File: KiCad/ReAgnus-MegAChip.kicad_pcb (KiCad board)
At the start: 4 copper layers, 78 x 49 mm, 55 parts, among them J1 Conn_02x05_Odd_Even, J2 Conn_02x02_Odd_Even, J3 Conn_01x03, J4 Conn_01x01, U1 PLCC-84-Plug, U11 74LVC245A, U12 74LVC1GX04, U13 TPS73643DBV, U2 LM1117-3.3, U3 SN74CBT16210, U4 SN74CBT16210, U5 SN74CBT16210, U6 SN74CBT16210, U7 GW1N-UV9LQ144, U8 74LVC1G07, U9 Agnus_TH_plug_pins, Y1 CL=16pF

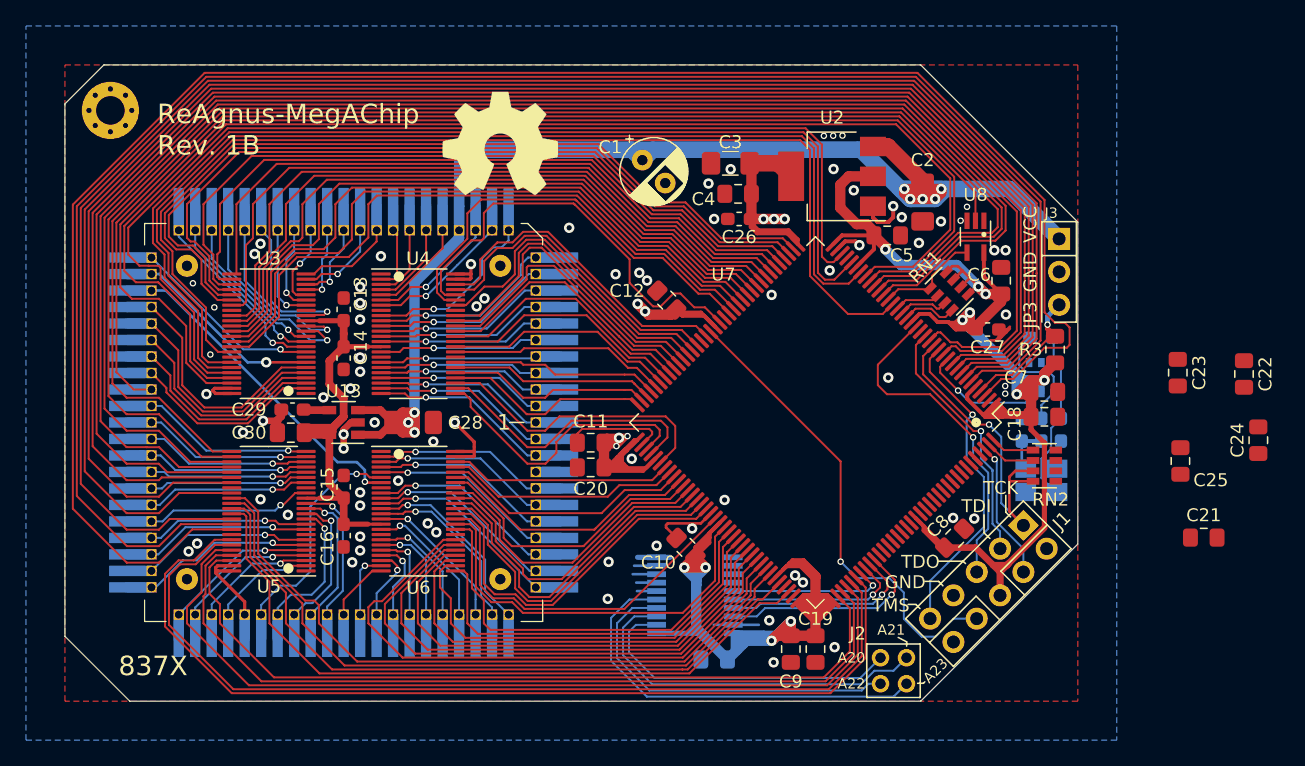
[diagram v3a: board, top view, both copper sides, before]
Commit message: Went to a 4-layer PCB and changed FPGA to GW1NR-UV9LQ144P with embedded PSRAM, changed FET-bus-switches to SN74CBT16210CDGVR (TVSOP-48) and added 4.3V LDO regulator TPS73643DBV and re-routed.
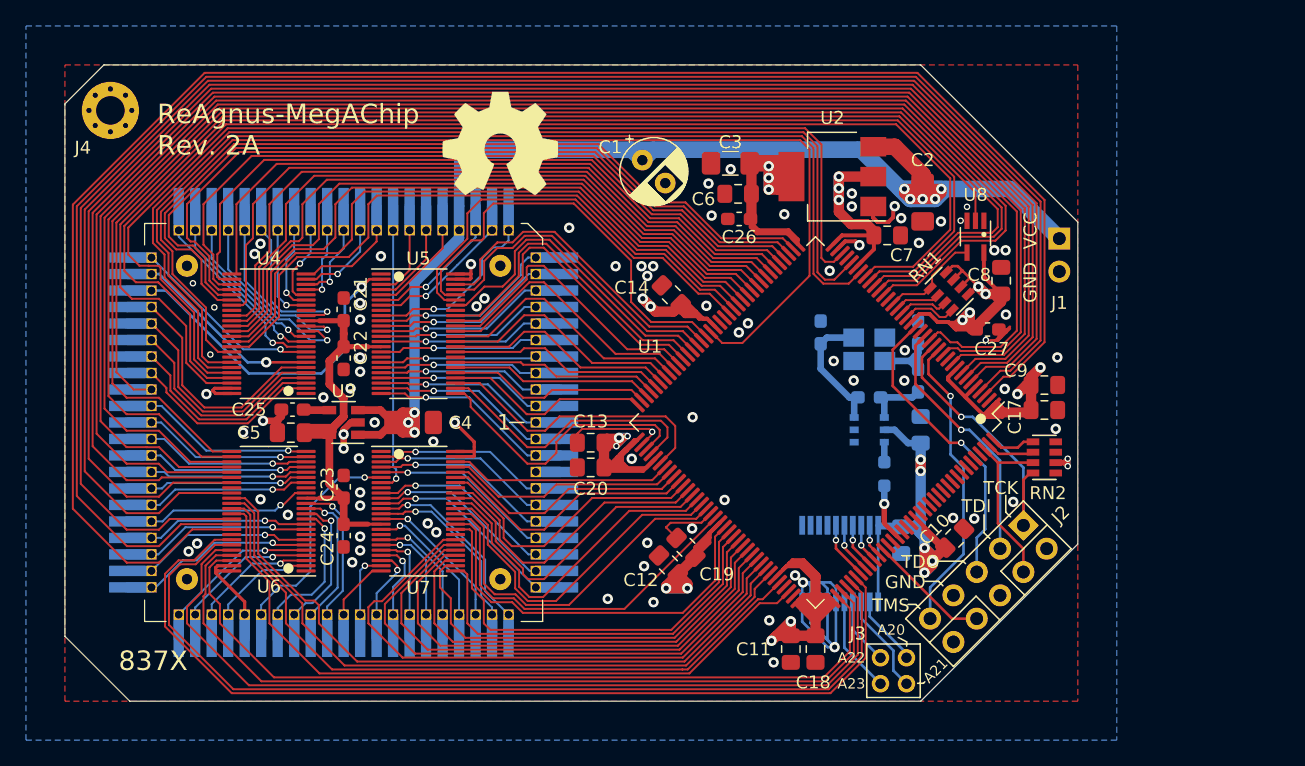
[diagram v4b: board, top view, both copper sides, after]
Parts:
- removed the C10 at (165.1, 124.5)
- removed the C11 at (157.8, 116.4)
- removed the C18 at (192.7, 114.4)
- removed the C23 at (203.0, 111.0)
- removed the C24 at (209.2, 116.2)
- removed the C25 at (203.2, 117.8)
- removed the C7 at (192.7, 112.5)
- removed the J3 at (193.9, 100.7)
- removed the U11 at (165.8, 128.1)
- removed the U12 at (192.5, 111.4)
- removed the U7 at (175.1, 114.8)
- added C13: 0.1uF, Capacitor_SMD:C_0805_2012Metric_Pad1.15x1.40mm_HandSolder, F.Cu at (157.8, 116.4)
- added C14: 0.1uF, Capacitor_SMD:C_0805_2012Metric_Pad1.15x1.40mm_HandSolder, F.Cu at (164.0, 105.0)
- added C15: 0.1uF, Capacitor_SMD:C_0805_2012Metric_Pad1.15x1.40mm_HandSolder, B.Cu at (181.7, 123.9)
- added C9: 0.1uF, Capacitor_SMD:C_0805_2012Metric_Pad1.15x1.40mm_HandSolder, F.Cu at (192.7, 112.0)
- added J1: Conn_01x02, Connector_PinHeader_2.54mm:PinHeader_1x02_P2.54mm_Vertical, F.Cu at (193.9, 100.7)
- added U1: GW1NR-UV9LQ144P, Package_QFP:LQFP-144_20x20mm_P0.5mm, F.Cu at (175.1, 114.8)
- added U10: 74LVC245A, Package_SO:TSSOP-20_4.4x6.5mm_P0.65mm, B.Cu at (177.0, 125.7)
- added U9: 74LVC1GX04, Package_SO:TSOP-6_1.65x3.05mm_P0.95mm, B.Cu at (179.2, 115.4)
- C16: renamed from C21; value 0.01uF -> 0.1uF; moved to B.Cu
- C17: value 0.1uF -> 0.01uF; moved to F.Cu
- C21: renamed from C13; value 0.1uF -> 0.1uF (0603)
- C22: renamed from C14; value 0.1uF -> 0.1uF (0603)
- C23: renamed from C15; value 0.1uF -> 0.1uF (0603)
- C24: renamed from C16; value 0.1uF -> 0.1uF (0603)
- C5: renamed from C30; value 10uF -> 1uF
- R3: value R_Small -> 33Ω; footprint Resistor_SMD:R_0805_2012Metric_Pad1.15x1.40mm_HandSolder -> Resistor_SMD:R_0603_1608Metric_Pad0.98x0.95mm_HandSolder; moved to B.Cu
- RN1, RN2: value R_Pack04 -> 4.7k
- moved C19 45.0 mm to (165.1, 124.5), turned to 135 degrees
- moved C17 31.9 mm to (192.7, 113.9), turned to 0 degrees
- moved C16 23.3 mm to (183.2, 115.4), turned to 90 degrees
- moved C12 20.4 mm to (163.8, 125.8)
- moved C29 20.0 mm to (175.5, 107.9), turned to 90 degrees
- moved Y1 16.7 mm to (179.2, 109.2), turned to 180 degrees
- moved R3 16.3 mm to (180.4, 118.8), turned to 270 degrees
- moved R2 14.0 mm to (179.2, 112.9), turned to 180 degrees
- moved C28 11.0 mm to (183.0, 107.9)
- moved R1 10.2 mm to (183.0, 111.6), turned to 90 degrees
- moved RN2 0.64 mm to (192.7, 117.5)
- renumbered C8 to C10, C9 to C11, C19 to C18, C22 to C19, C29 to C25, C41 to C28, C40 to C29, C28 to C4, C4 to C6, C5 to C7, C6 to C8, J1 to J2, J2 to J3, U1 to U11, U9 to U12, U13 to U3, U3 to U4, U4 to U5, U5 to U6, U6 to U7
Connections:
- J2 pad 4: JP1 -> nNTSC
- J2 pad 8: JP2 -> JP1
- J3 pad 1: A20 -> A22
- J3 pad 2: A21 -> A20
- J3 pad 3: A22 -> A23
- J3 pad 4: A23 -> A21
- R3 pad 1: 3V3 -> Net-(R3-Pad1)
- R3 pad 2: JP3 -> GCLKT_1
- RN2 pad 3: TCK -> nNTSC
- RN2 pad 6: GND -> 3V3
- U5 pad 2: BLISS -> XCLK|A20
- U5 pad 46: BLISS_3V3 -> XCLK|A20_3V3
- U7 pad 40: XCLK|A20_3V3 -> BLISS_3V3
- U7 pad 7: XCLK|A20 -> BLISS
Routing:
- net JP2: track 36.5 -> 0.00 mm, vias 1 -> 0
- net 3V3: track 288.6 -> 262.3 mm, vias 19 -> 28
- net A23: track 31.7 -> 7.46 mm
- net A22: track 27.8 -> 5.19 mm
- net A21: track 28.7 -> 7.75 mm
- net GND: track 65.7 -> 86.3 mm, vias 76 -> 85
- net A20: track 24.8 -> 5.48 mm
- net BLISS: track 6.88 -> 22.8 mm, vias 0 -> 1
- net nNTSC: track 0.00 -> 13.4 mm
- net A20_3V3: track 16.4 -> 3.08 mm
- net A21_3V3: track 15.0 -> 3.52 mm
- net JP3: track 10.6 -> 0.00 mm, vias 1 -> 0
- net GCLKT_7: track 9.71 -> 0.00 mm, vias 1 -> 0
- net A22_3V3: track 13.6 -> 4.00 mm
- net GCLKT_1: track 0.00 -> 8.58 mm, vias 0 -> 1
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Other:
- board text added: "(C) 2022, 2024 Design by J.Bilander"
- board text added: "33Ω"
- board text added: "ReAgnus-MegAChip Rev. 2A"
- board text removed: "(C) 2022 Design by J.Bilander"
- board text removed: "JP3"
- board text removed: "ReAgnus-MegAChip Rev. 1B"

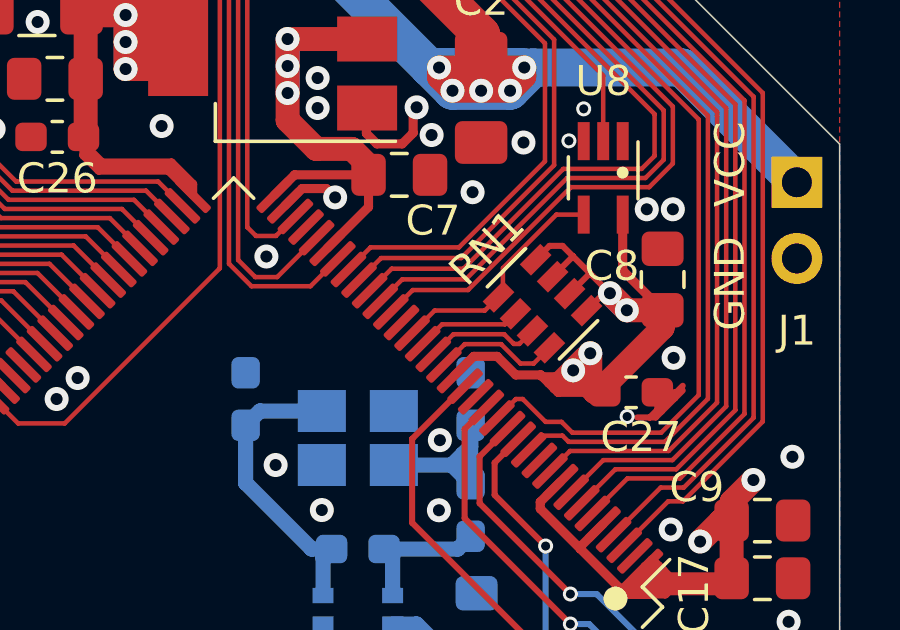
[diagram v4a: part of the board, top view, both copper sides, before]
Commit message: Moved signal nNTSC_8372_3V3 to pin FPGA pin 24
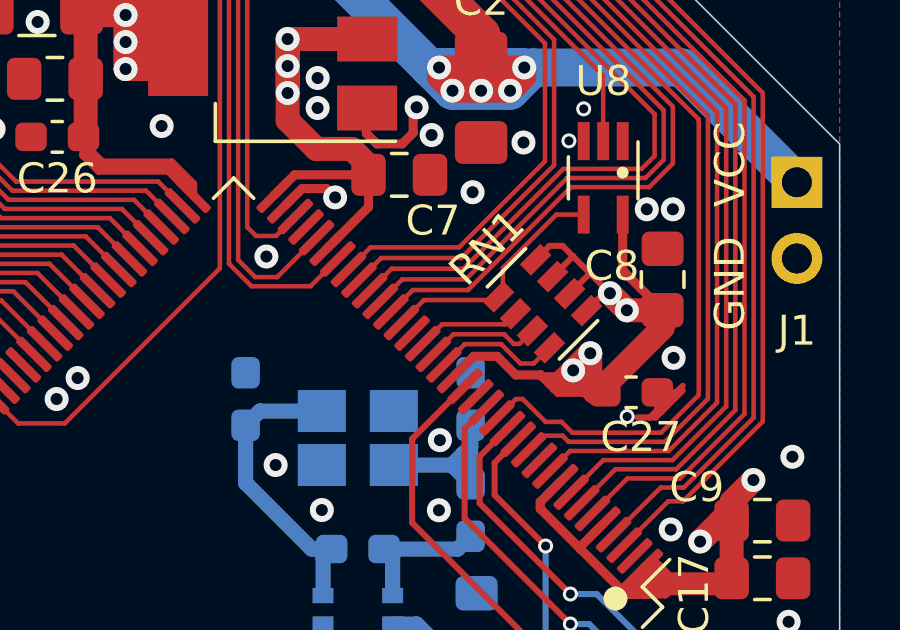
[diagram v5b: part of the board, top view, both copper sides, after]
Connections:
- U1 pad 23: nNTSC_8372_3V3 -> Net-(U1-Pad23)
- U1 pad 24: Net-(U1-Pad24) -> nNTSC_8372_3V3

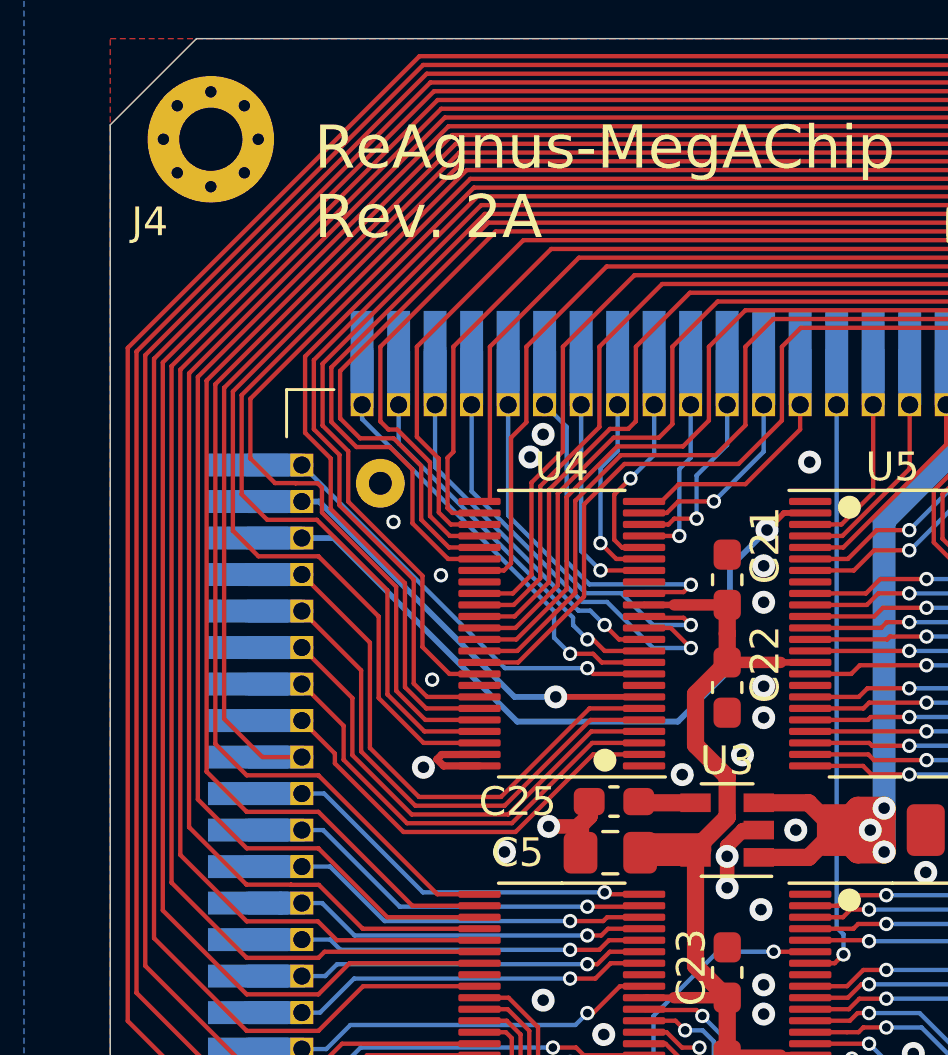
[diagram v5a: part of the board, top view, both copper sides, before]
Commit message: Added a pull-up resistor R4 for pin 41 (PAL/NTSC-selector) because A500 Rev.6A doesn't have pull-up on motherboard, and bumped to Rev. 2B
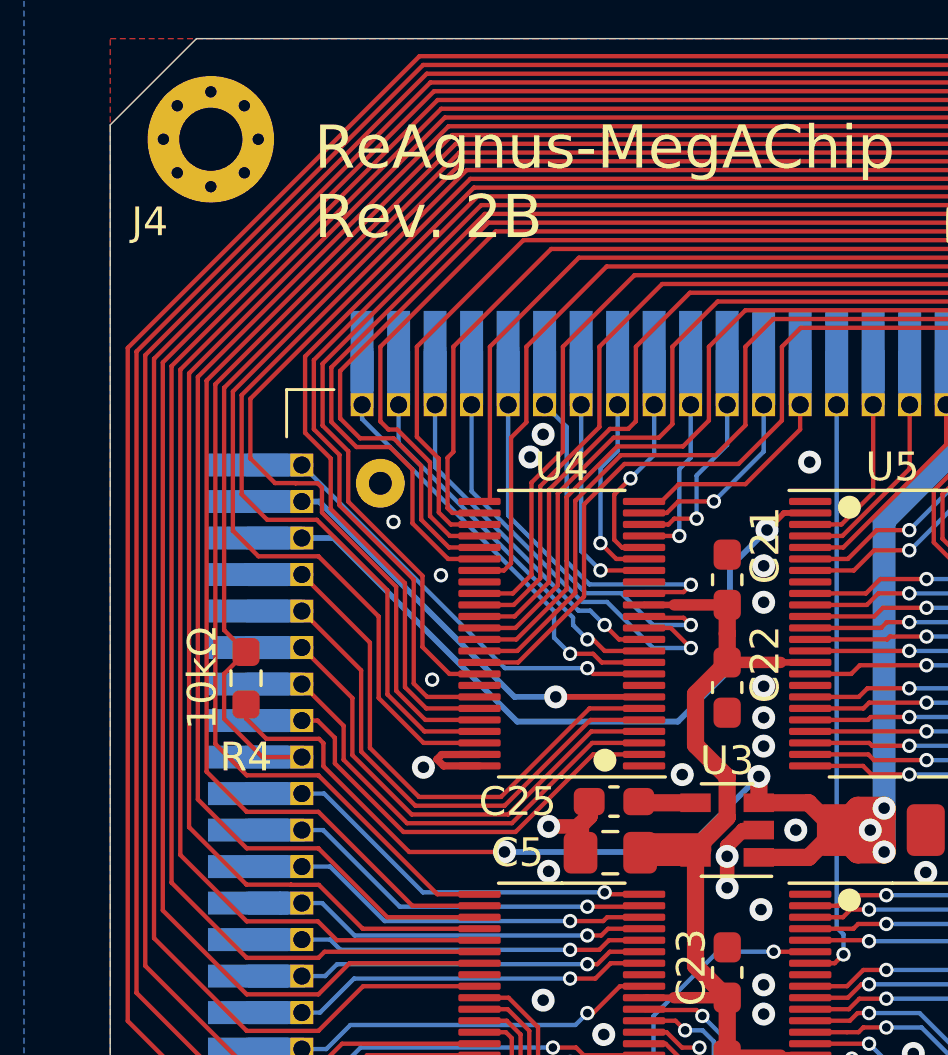
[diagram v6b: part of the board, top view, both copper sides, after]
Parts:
- added R4: 10kΩ, Resistor_SMD:R_0603_1608Metric_Pad0.98x0.95mm_HandSolder, F.Cu at (122.0, 109.6)
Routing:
- net VCC: track 146.4 -> 169.1 mm, vias 8 -> 10
- net GND|nNTSC_8372: track 90.8 -> 91.4 mm
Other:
- board text added: "10kΩ"
- board text added: "ReAgnus-MegAChip Rev. 2B"
- board text removed: "ReAgnus-MegAChip Rev. 2A"

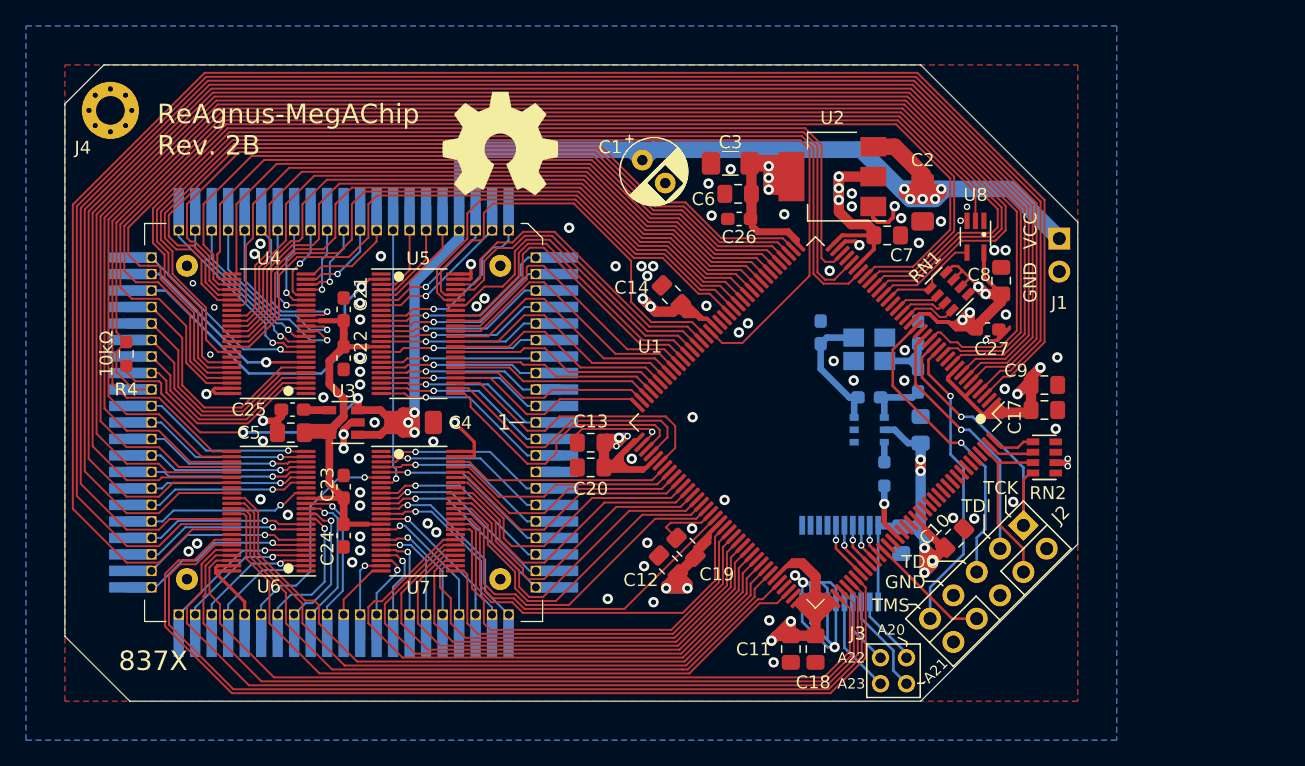
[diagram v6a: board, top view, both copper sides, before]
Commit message: Moved signals from bank 3 to bank 0
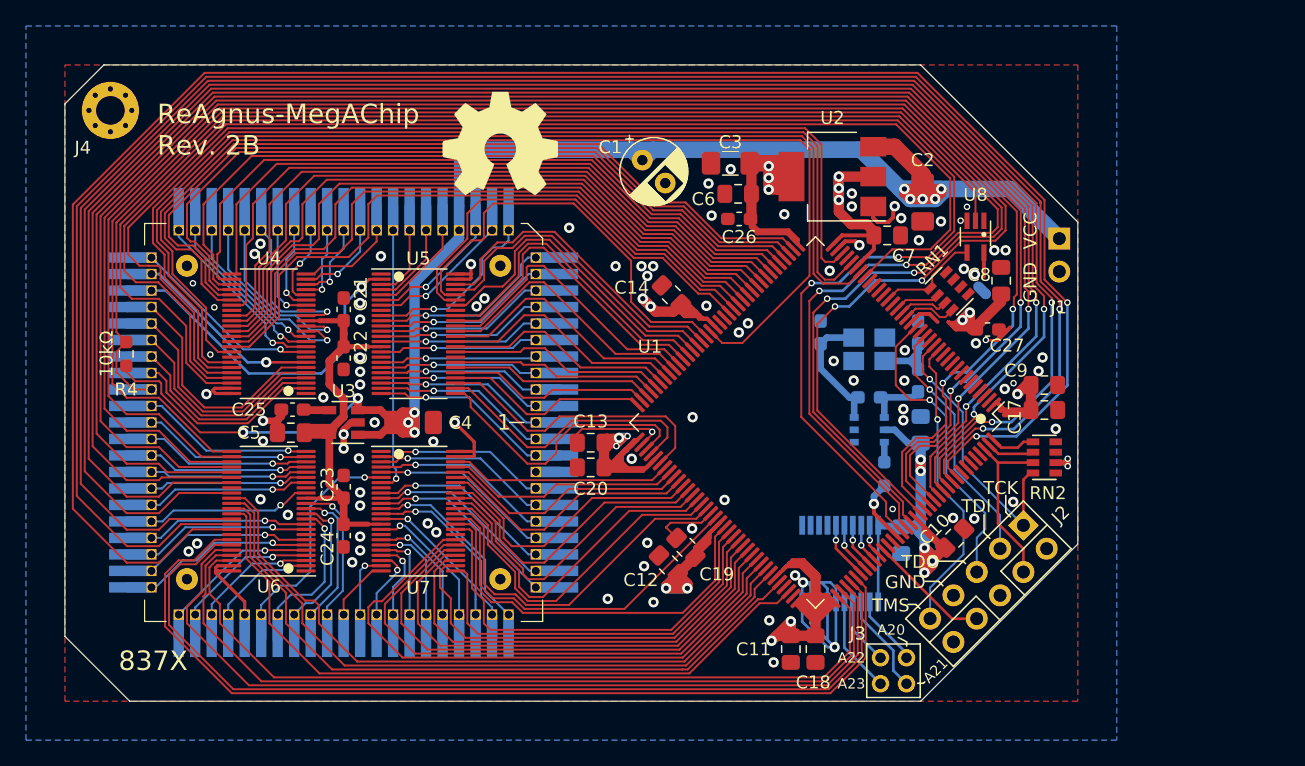
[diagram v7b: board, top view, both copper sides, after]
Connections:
- U1 pad 10: DRA5|DRA4_3V3 -> Net-(U1-Pad10)
- U1 pad 12: DRA4|DRA3_3V3 -> Net-(U1-Pad12)
- U1 pad 124: Net-(U1-Pad124) -> 14M|CCK_3V3
- U1 pad 125: Net-(U1-Pad125) -> DRA0_3V3|GND
- U1 pad 126: Net-(U1-Pad126) -> DRA1|DRA0_3V3
- U1 pad 128: Net-(U1-Pad128) -> DRA2|DRA1_3V3
- U1 pad 129: Net-(U1-Pad129) -> DRA3|DRA2_3V3
- U1 pad 130: Net-(U1-Pad130) -> DRA4|DRA3_3V3
- U1 pad 131: Net-(U1-Pad131) -> DRA5|DRA4_3V3
- U1 pad 132: Net-(U1-Pad132) -> DRA6|DRA5_3V3
- U1 pad 133: Net-(U1-Pad133) -> DRA7|DRA6_3V3
- U1 pad 134: Net-(U1-Pad134) -> DRA8|DRA7_3V3
- U1 pad 135: Net-(U1-Pad135) -> DRA8|LDS_3V3
- U1 pad 136: Net-(U1-Pad136) -> LDS|UDS_3V3
- U1 pad 15: DRA3|DRA2_3V3 -> Net-(U1-Pad15)
- U1 pad 19: 3V3 -> 1V8
- U1 pad 25: DRA2|DRA1_3V3 -> Net-(U1-Pad25)
- U1 pad 26: DRA1|DRA0_3V3 -> Net-(U1-Pad26)
- U1 pad 27: DRA0_3V3|GND -> Net-(U1-Pad27)
- U1 pad 28: 14M|CCK_3V3 -> Net-(U1-Pad28)
- U1 pad 3: LDS|UDS_3V3 -> Net-(U1-Pad3)
- U1 pad 4: DRA8|LDS_3V3 -> Net-(U1-Pad4)
- U1 pad 5: 3V3 -> 1V8
- U1 pad 6: DRA8|DRA7_3V3 -> Net-(U1-Pad6)
- U1 pad 7: DRA7|DRA6_3V3 -> Net-(U1-Pad7)
- U1 pad 8: DRA6|DRA5_3V3 -> Net-(U1-Pad8)
- U1 pad 9: 3V3 -> 1V8
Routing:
- net 3V3: track 262.3 -> 233.5 mm
- net 14M|CCK_3V3: track 99.8 -> 127.0 mm, vias 0 -> 2
- net DRA0_3V3|GND: track 111.3 -> 137.4 mm, vias 0 -> 2
- net DRA1|DRA0_3V3: track 113.6 -> 138.6 mm, vias 0 -> 2
- net DRA2|DRA1_3V3: track 115.8 -> 139.7 mm, vias 0 -> 2
- net DRA4|DRA3_3V3: track 123.3 -> 135.1 mm, vias 0 -> 2
- net DRA3|DRA2_3V3: track 122.3 -> 133.9 mm, vias 0 -> 2
- net DRA5|DRA4_3V3: track 125.4 -> 137.0 mm, vias 0 -> 2
- net DRA8|LDS_3V3: track 135.9 -> 146.8 mm, vias 0 -> 2
- net LDS|UDS_3V3: track 138.8 -> 149.6 mm, vias 0 -> 2
- net DRA8|DRA7_3V3: track 133.1 -> 143.9 mm, vias 0 -> 2
- net DRA6|DRA5_3V3: track 128.1 -> 137.9 mm, vias 0 -> 2
- net DRA7|DRA6_3V3: track 130.9 -> 140.4 mm, vias 0 -> 2
- net GCLKT_1: track 8.58 -> 4.98 mm
- net 1V8: track 0.00 -> 2.56 mm
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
